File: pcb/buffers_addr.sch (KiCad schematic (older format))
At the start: 24 parts, among them U3 74LVCH162245A, U4 74LVCH162245A

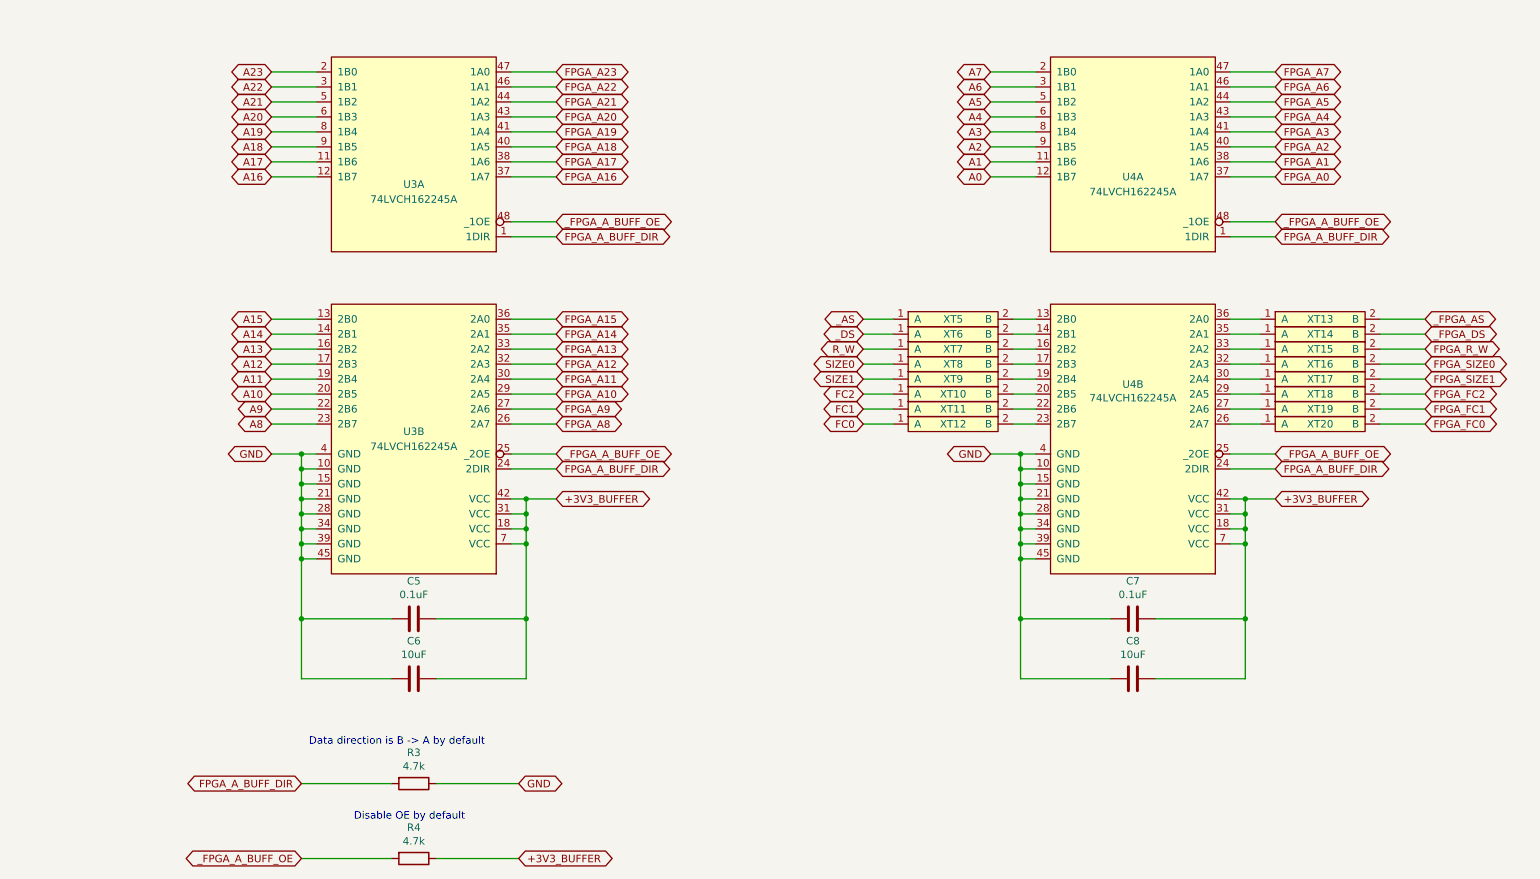
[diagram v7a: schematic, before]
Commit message: more footprints assigned
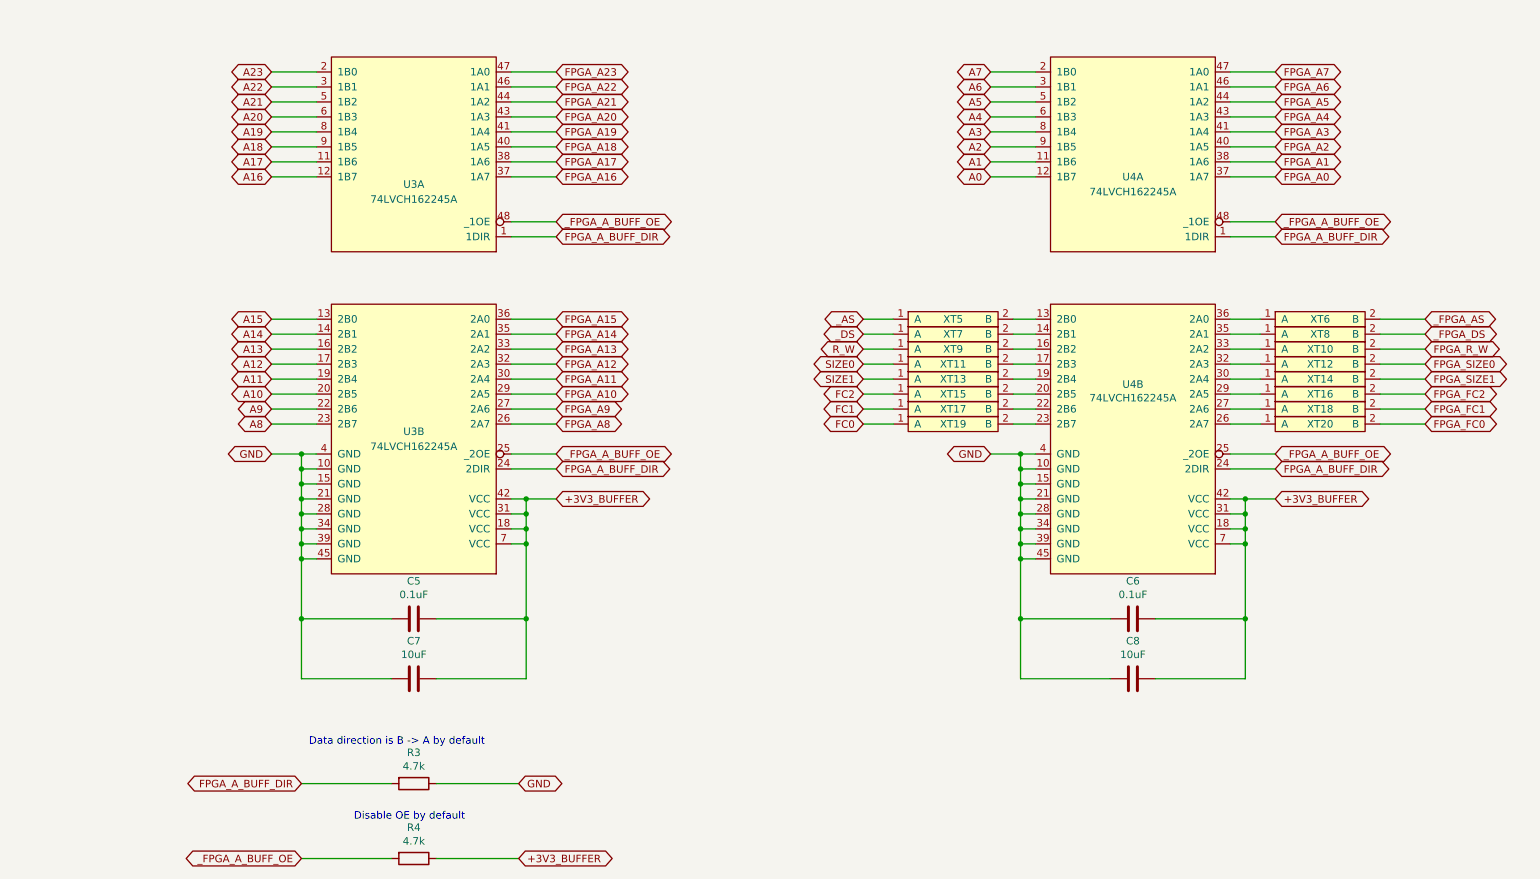
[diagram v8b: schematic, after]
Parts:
- U3, U4: footprint (none) -> Package_SO:TSSOP-48_6.1x12.5mm_P0.5mm
- XT10: renamed from XT15; footprint (none) -> WM1200:testpoint_cutline
- XT11: renamed from XT8; footprint (none) -> WM1200:testpoint_cutline
- XT12: renamed from XT16; footprint (none) -> WM1200:testpoint_cutline
- XT13: renamed from XT9; footprint (none) -> WM1200:testpoint_cutline
- XT14: renamed from XT17; footprint (none) -> WM1200:testpoint_cutline
- XT15: renamed from XT10; footprint (none) -> WM1200:testpoint_cutline
- XT16: renamed from XT18; footprint (none) -> WM1200:testpoint_cutline
- XT17: renamed from XT11; footprint (none) -> WM1200:testpoint_cutline
- XT18: renamed from XT19; footprint (none) -> WM1200:testpoint_cutline
- XT19: renamed from XT12; footprint (none) -> WM1200:testpoint_cutline
- XT20, XT5: footprint (none) -> WM1200:testpoint_cutline
- XT6: renamed from XT13; footprint (none) -> WM1200:testpoint_cutline
- XT7: renamed from XT6; footprint (none) -> WM1200:testpoint_cutline
- XT8: renamed from XT14; footprint (none) -> WM1200:testpoint_cutline
- XT9: renamed from XT7; footprint (none) -> WM1200:testpoint_cutline
- renumbered C7 to C6, C6 to C7
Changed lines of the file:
@@
 F 0 "U3" H 3250 3200 50  0000 C CNN
 F 1 "74LVCH162245A" H 3250 3100 50  0000 C CNN
-F 2 "" H 3250 2750 50  0001 C CNN
+F 2 "Package_SO:TSSOP-48_6.1x12.5mm_P0.5mm" H 3250 2750 50  0001 C CNN
 F 3 "" H 3250 2750 50  0001 C CNN
 	1    3250 2750
@@
 F 0 "U3" H 3250 5850 50  0000 C CNN
 F 1 "74LVCH162245A" H 3250 5750 50  0000 C CNN
-F 2 "" H 3250 4900 50  0001 C CNN
+F 2 "Package_SO:TSSOP-48_6.1x12.5mm_P0.5mm" H 3250 4900 50  0001 C CNN
 F 3 "" H 3250 4900 50  0001 C CNN
 	2    3250 4900
@@
 F 0 "U4" H 8050 3250 50  0000 C CNN
 F 1 "74LVCH162245A" H 8050 3150 50  0000 C CNN
-F 2 "" H 8050 2750 50  0001 C CNN
+F 2 "Package_SO:TSSOP-48_6.1x12.5mm_P0.5mm" H 8050 2750 50  0001 C CNN
 F 3 "" H 8050 2750 50  0001 C CNN
 	1    8050 2750
@@
 F 0 "U4" H 8050 6165 50  0000 C CNN
 F 1 "74LVCH162245A" H 8050 6074 50  0000 C CNN
-F 2 "" H 8050 4900 50  0001 C CNN
+F 2 "Package_SO:TSSOP-48_6.1x12.5mm_P0.5mm" H 8050 4900 50  0001 C CNN
 F 3 "" H 8050 4900 50  0001 C CNN
 	2    8050 4900
@@
 	8700 4600 8800 4600
 $Comp
-L Device:C C6
+L Device:C C7
 U 1 1 5E91F422
 P 3250 5600
-F 0 "C6" V 3502 5600 50  0000 C CNN
+F 0 "C7" V 3502 5600 50  0000 C CNN
 F 1 "10uF" V 3411 5600 50  0000 C CNN
 F 2 "" H 3288 5450 50  0001 C CNN
@@
 $EndComp
 $Comp
-L Device:C C7
+L Device:C C6
 U 1 1 5E91F427
 P 8050 5200
-F 0 "C7" V 8302 5200 50  0000 C CNN
+F 0 "C6" V 8302 5200 50  0000 C CNN
 F 1 "0.1uF" V 8211 5200 50  0000 C CNN
 F 2 "" H 8088 5050 50  0001 C CNN
@@
 F 0 "XT5" H 6850 3300 50  0000 C CNN
 F 1 "testpoint_cutline" H 6850 3400 50  0001 C CNN
-F 2 "" H 7000 3250 50  0001 C CNN
+F 2 "WM1200:testpoint_cutline" H 7000 3250 50  0001 C CNN
 F 3 "" H 7000 3250 50  0001 C CNN
 	1    6850 3250
@@
 $EndComp
 $Comp
-L WM1200:testpoint_cutline XT6
+L WM1200:testpoint_cutline XT7
 U 1 1 5E57D0C2
 P 6850 3350
-F 0 "XT6" H 6850 3400 50  0000 C CNN
+F 0 "XT7" H 6850 3400 50  0000 C CNN
 F 1 "testpoint_cutline" H 6850 3500 50  0001 C CNN
-F 2 "" H 7000 3350 50  0001 C CNN
+F 2 "WM1200:testpoint_cutline" H 7000 3350 50  0001 C CNN
 F 3 "" H 7000 3350 50  0001 C CNN
 	1    6850 3350
@@
 $EndComp
 $Comp
-L WM1200:testpoint_cutline XT7
+L WM1200:testpoint_cutline XT9
 U 1 1 5E57DCF2
 P 6850 3450
-F 0 "XT7" H 6850 3500 50  0000 C CNN
+F 0 "XT9" H 6850 3500 50  0000 C CNN
 F 1 "testpoint_cutline" H 6850 3600 50  0001 C CNN
-F 2 "" H 7000 3450 50  0001 C CNN
+F 2 "WM1200:testpoint_cutline" H 7000 3450 50  0001 C CNN
 F 3 "" H 7000 3450 50  0001 C CNN
 	1    6850 3450
@@
 $EndComp
 $Comp
-L WM1200:testpoint_cutline XT8
+L WM1200:testpoint_cutline XT11
 U 1 1 5E57E315
 P 6850 3550
-F 0 "XT8" H 6850 3600 50  0000 C CNN
+F 0 "XT11" H 6850 3600 50  0000 C CNN
 F 1 "testpoint_cutline" H 6850 3700 50  0001 C CNN
-F 2 "" H 7000 3550 50  0001 C CNN
+F 2 "WM1200:testpoint_cutline" H 7000 3550 50  0001 C CNN
 F 3 "" H 7000 3550 50  0001 C CNN
 	1    6850 3550
@@
 $EndComp
 $Comp
-L WM1200:testpoint_cutline XT9
+L WM1200:testpoint_cutline XT13
 U 1 1 5E57E966
 P 6850 3650
-F 0 "XT9" H 6850 3700 50  0000 C CNN
+F 0 "XT13" H 6850 3700 50  0000 C CNN
 F 1 "testpoint_cutline" H 6850 3800 50  0001 C CNN
-F 2 "" H 7000 3650 50  0001 C CNN
+F 2 "WM1200:testpoint_cutline" H 7000 3650 50  0001 C CNN
 F 3 "" H 7000 3650 50  0001 C CNN
 	1    6850 3650
@@
 $EndComp
 $Comp
-L WM1200:testpoint_cutline XT10
+L WM1200:testpoint_cutline XT15
 U 1 1 5E57EE80
 P 6850 3750
-F 0 "XT10" H 6850 3800 50  0000 C CNN
+F 0 "XT15" H 6850 3800 50  0000 C CNN
 F 1 "testpoint_cutline" H 6850 3900 50  0001 C CNN
-F 2 "" H 7000 3750 50  0001 C CNN
+F 2 "WM1200:testpoint_cutline" H 7000 3750 50  0001 C CNN
 F 3 "" H 7000 3750 50  0001 C CNN
 	1    6850 3750
@@
 $EndComp
 $Comp
-L WM1200:testpoint_cutline XT11
+L WM1200:testpoint_cutline XT17
 U 1 1 5E57F468
 P 6850 3850
-F 0 "XT11" H 6850 3900 50  0000 C CNN
+F 0 "XT17" H 6850 3900 50  0000 C CNN
 F 1 "testpoint_cutline" H 6850 4000 50  0001 C CNN
-F 2 "" H 7000 3850 50  0001 C CNN
+F 2 "WM1200:testpoint_cutline" H 7000 3850 50  0001 C CNN
 F 3 "" H 7000 3850 50  0001 C CNN
 	1    6850 3850
@@
 $EndComp
 $Comp
-L WM1200:testpoint_cutline XT12
+L WM1200:testpoint_cutline XT19
 U 1 1 5E57FB7E
 P 6850 3950
-F 0 "XT12" H 6850 4000 50  0000 C CNN
+F 0 "XT19" H 6850 4000 50  0000 C CNN
 F 1 "testpoint_cutline" H 6850 4100 50  0001 C CNN
-F 2 "" H 7000 3950 50  0001 C CNN
+F 2 "WM1200:testpoint_cutline" H 7000 3950 50  0001 C CNN
 F 3 "" H 7000 3950 50  0001 C CNN
 	1    6850 3950
@@
 Data direction is B -> A by default
 $Comp
-L WM1200:testpoint_cutline XT13
+L WM1200:testpoint_cutline XT6
 U 1 1 5EA42E26
 P 9300 3250
-F 0 "XT13" H 9300 3300 50  0000 C CNN
+F 0 "XT6" H 9300 3300 50  0000 C CNN
 F 1 "testpoint_cutline" H 9300 3400 50  0001 C CNN
-F 2 "" H 9450 3250 50  0001 C CNN
+F 2 "WM1200:testpoint_cutline" H 9450 3250 50  0001 C CNN
 F 3 "" H 9450 3250 50  0001 C CNN
 	1    9300 3250
@@
 $EndComp
 $Comp
-L WM1200:testpoint_cutline XT14
+L WM1200:testpoint_cutline XT8
 U 1 1 5EA42E2C
 P 9300 3350
-F 0 "XT14" H 9300 3400 50  0000 C CNN
+F 0 "XT8" H 9300 3400 50  0000 C CNN
 F 1 "testpoint_cutline" H 9300 3500 50  0001 C CNN
-F 2 "" H 9450 3350 50  0001 C CNN
+F 2 "WM1200:testpoint_cutline" H 9450 3350 50  0001 C CNN
 F 3 "" H 9450 3350 50  0001 C CNN
 	1    9300 3350
@@
 $EndComp
 $Comp
-L WM1200:testpoint_cutline XT15
+L WM1200:testpoint_cutline XT10
 U 1 1 5EA42E32
 P 9300 3450
-F 0 "XT15" H 9300 3500 50  0000 C CNN
+F 0 "XT10" H 9300 3500 50  0000 C CNN
 F 1 "testpoint_cutline" H 9300 3600 50  0001 C CNN
-F 2 "" H 9450 3450 50  0001 C CNN
+F 2 "WM1200:testpoint_cutline" H 9450 3450 50  0001 C CNN
 F 3 "" H 9450 3450 50  0001 C CNN
 	1    9300 3450
@@
 $EndComp
 $Comp
-L WM1200:testpoint_cutline XT16
+L WM1200:testpoint_cutline XT12
 U 1 1 5EA42E38
 P 9300 3550
-F 0 "XT16" H 9300 3600 50  0000 C CNN
+F 0 "XT12" H 9300 3600 50  0000 C CNN
 F 1 "testpoint_cutline" H 9300 3700 50  0001 C CNN
-F 2 "" H 9450 3550 50  0001 C CNN
+F 2 "WM1200:testpoint_cutline" H 9450 3550 50  0001 C CNN
 F 3 "" H 9450 3550 50  0001 C CNN
 	1    9300 3550
@@
 $EndComp
 $Comp
-L WM1200:testpoint_cutline XT17
+L WM1200:testpoint_cutline XT14
 U 1 1 5EA42E3E
 P 9300 3650
-F 0 "XT17" H 9300 3700 50  0000 C CNN
+F 0 "XT14" H 9300 3700 50  0000 C CNN
 F 1 "testpoint_cutline" H 9300 3800 50  0001 C CNN
-F 2 "" H 9450 3650 50  0001 C CNN
+F 2 "WM1200:testpoint_cutline" H 9450 3650 50  0001 C CNN
 F 3 "" H 9450 3650 50  0001 C CNN
 	1    9300 3650
@@
 $EndComp
 $Comp
-L WM1200:testpoint_cutline XT18
+L WM1200:testpoint_cutline XT16
 U 1 1 5EA42E44
 P 9300 3750
-F 0 "XT18" H 9300 3800 50  0000 C CNN
+F 0 "XT16" H 9300 3800 50  0000 C CNN
 F 1 "testpoint_cutline" H 9300 3900 50  0001 C CNN
-F 2 "" H 9450 3750 50  0001 C CNN
+F 2 "WM1200:testpoint_cutline" H 9450 3750 50  0001 C CNN
 F 3 "" H 9450 3750 50  0001 C CNN
 	1    9300 3750
@@
 $EndComp
 $Comp
-L WM1200:testpoint_cutline XT19
+L WM1200:testpoint_cutline XT18
 U 1 1 5EA42E4A
 P 9300 3850
-F 0 "XT19" H 9300 3900 50  0000 C CNN
+F 0 "XT18" H 9300 3900 50  0000 C CNN
 F 1 "testpoint_cutline" H 9300 4000 50  0001 C CNN
-F 2 "" H 9450 3850 50  0001 C CNN
+F 2 "WM1200:testpoint_cutline" H 9450 3850 50  0001 C CNN
 F 3 "" H 9450 3850 50  0001 C CNN
 	1    9300 3850
@@
 F 0 "XT20" H 9300 4000 50  0000 C CNN
 F 1 "testpoint_cutline" H 9300 4100 50  0001 C CNN
-F 2 "" H 9450 3950 50  0001 C CNN
+F 2 "WM1200:testpoint_cutline" H 9450 3950 50  0001 C CNN
 F 3 "" H 9450 3950 50  0001 C CNN
 	1    9300 3950
